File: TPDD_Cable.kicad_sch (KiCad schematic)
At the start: 5 parts

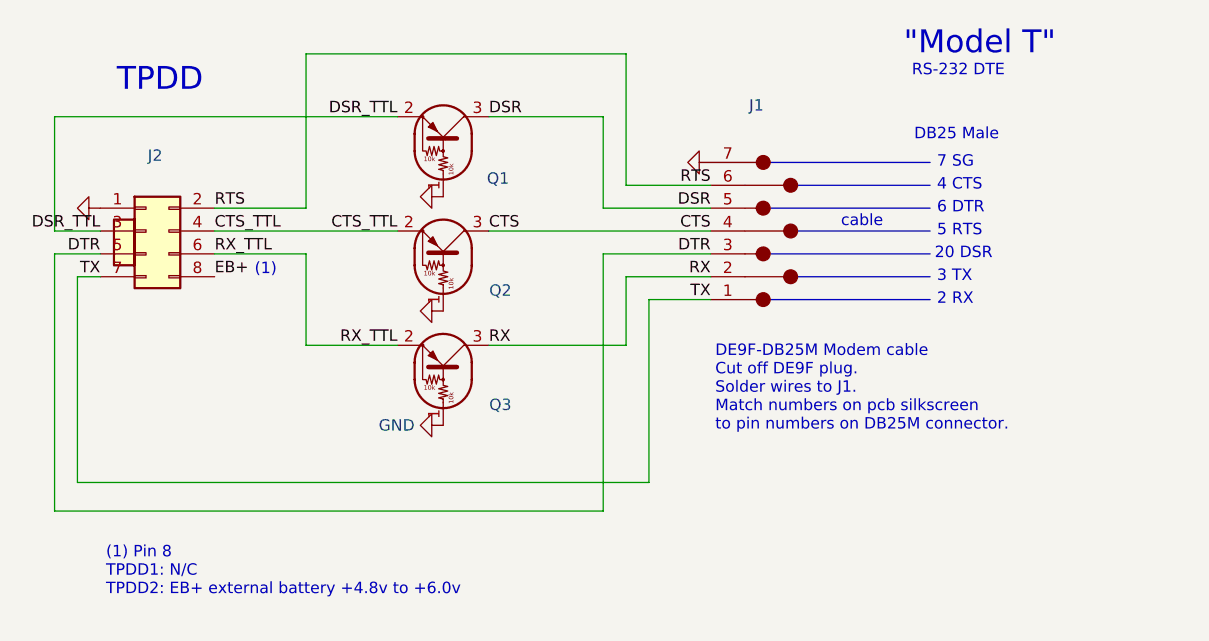
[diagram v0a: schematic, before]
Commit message: add cable tests to readme
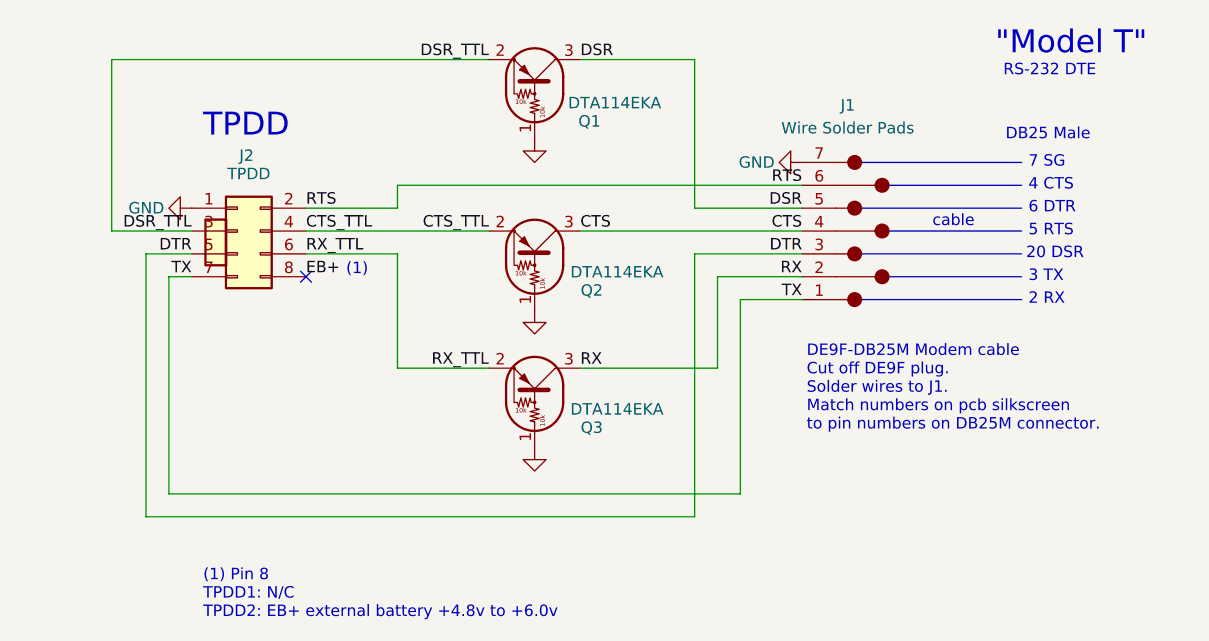
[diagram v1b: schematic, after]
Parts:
- J1: value (none) -> Wire Solder Pads; footprint (none) -> 000_LOCAL:D7_1.5mm_wirepads
- J2: value (none) -> TPDD; footprint (none) -> 000_LOCAL:2-6-2_tpdd
- Q1, Q2, Q3: value (none) -> DTA114EKA; footprint (none) -> 000_LOCAL:SC-59
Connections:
- no-connect marks 0 -> 1
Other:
- moved on the sheet: J1, J2, Q1, Q2, Q3
